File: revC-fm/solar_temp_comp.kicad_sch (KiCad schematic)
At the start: 19 parts, among them U35 ATL431BQ, U36 LT6004HMS8, U37 LT3010-5, U38 ATL431BQ

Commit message: routing
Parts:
- C139: renamed from C125; footprint Capacitor_SMD:C_0402_1005Metric -> Capacitor_SMD:C_0603_1608Metric
- renumbered C122 to C136, C123 to C137, C124 to C138, R246 to R237, R253 to R238, R243 to R239, R248 to R240, R244 to R241, R249 to R242, R245 to R243, R250 to R244, U37 to U38, U36 to U39, U35 to U40, U38 to U41

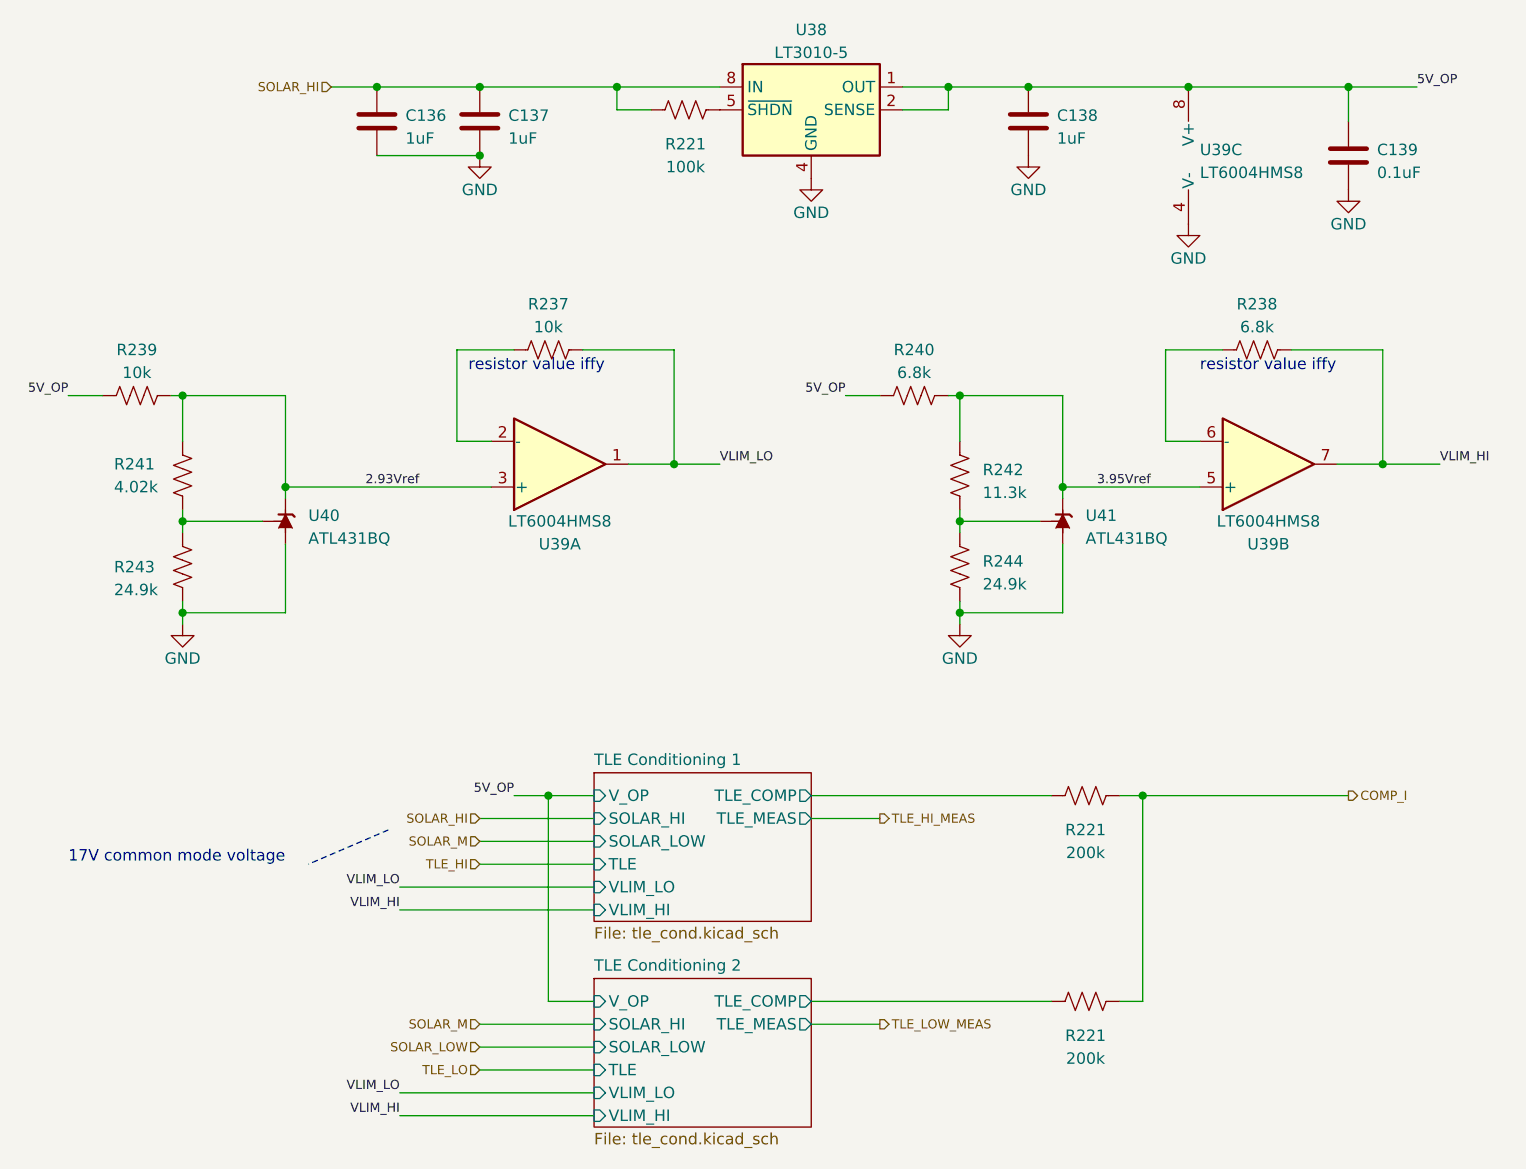
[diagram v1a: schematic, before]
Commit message: changed RF connector to TH
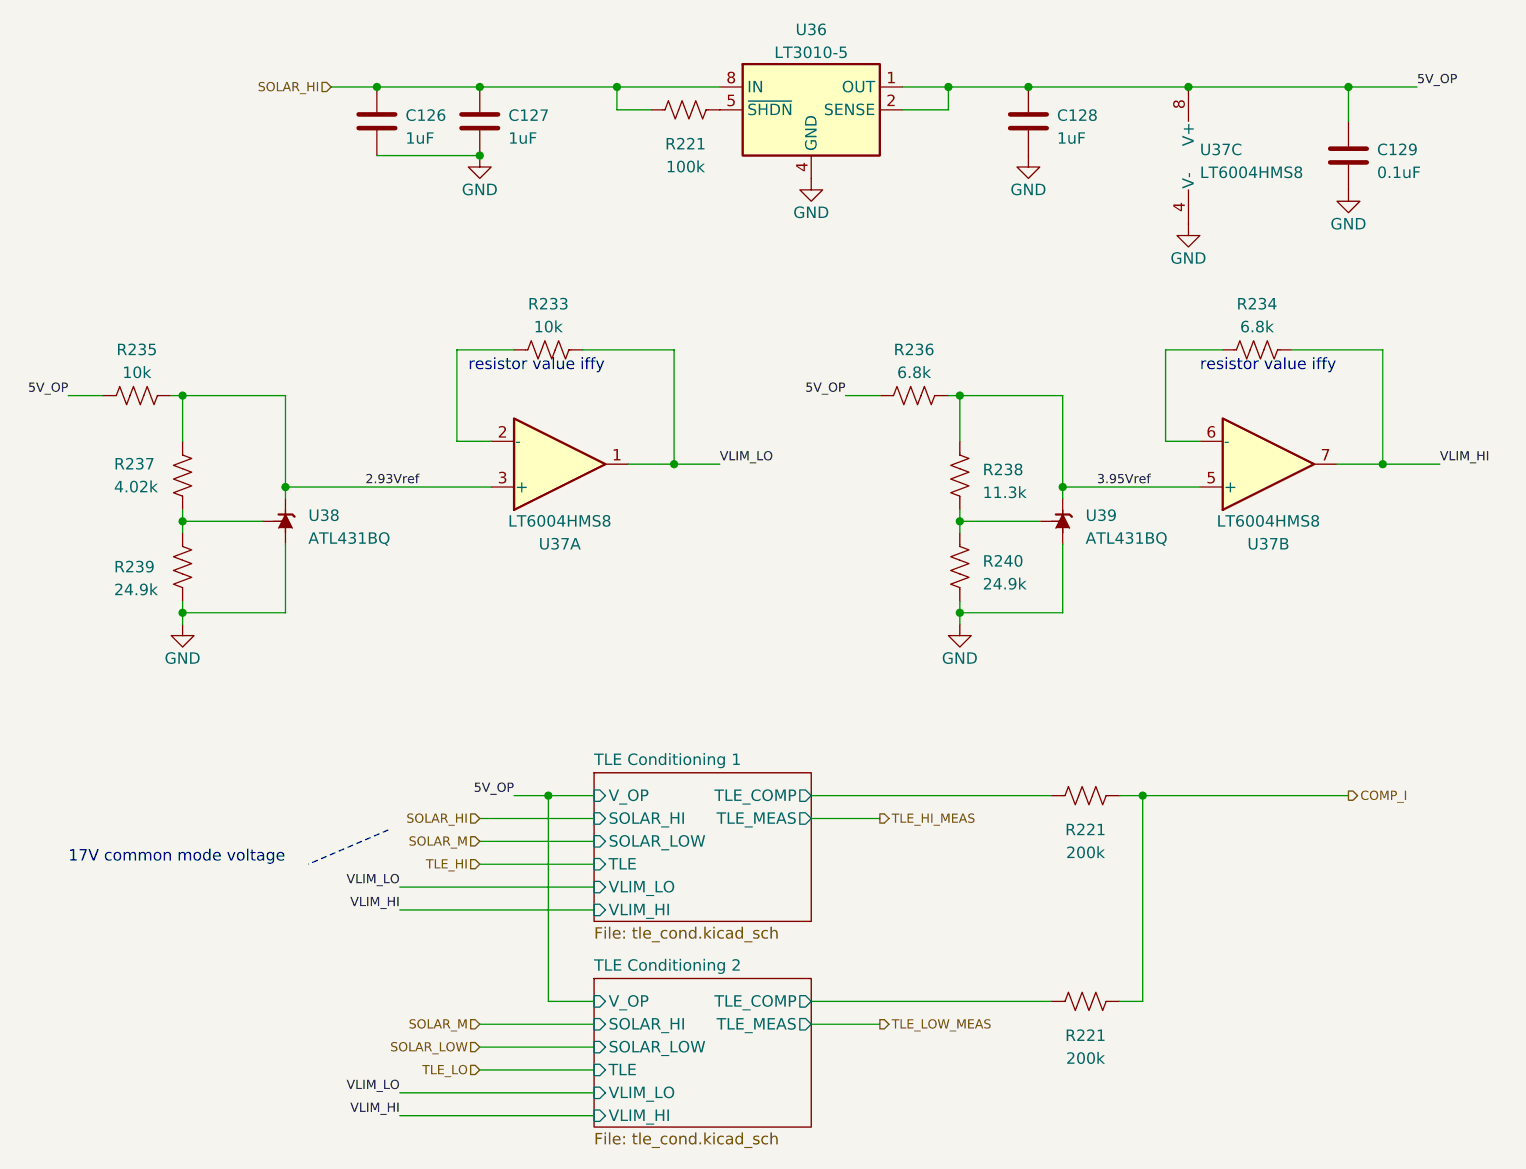
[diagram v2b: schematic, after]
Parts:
- renumbered C136 to C126, C137 to C127, C138 to C128, C139 to C129, R237 to R233, R238 to R234, R239 to R235, R240 to R236, R241 to R237, R242 to R238, R243 to R239, R244 to R240, U38 to U36, U39 to U37, U40 to U38, U41 to U39

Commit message: working revC review changes
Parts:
- renumbered C126 to C127, C127 to C128, C128 to C129, C129 to C130, R233 to R250, R234 to R251, R235 to R252, R236 to R253, R237 to R254, R238 to R255, R239 to R256, R240 to R257, U36 to U37, U37 to U38, U38 to U39, U39 to U40

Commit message: working revC
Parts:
- removed C127, C128: 1uF, Capacitor_SMD:C_0805_2012Metric, symbol Device:C
- removed C129: 1uF, Capacitor_SMD:C_0603_1608Metric, symbol Device:C
- removed C130: 0.1uF, Capacitor_SMD:C_0603_1608Metric, symbol Device:C
- removed R221: 100k, Resistor_SMD:R_0603_1608Metric, symbol Device:R_US
- removed R221: 200k, Resistor_SMD:R_0603_1608Metric, symbol Device:R_US
- removed R250, R252: 10k, Resistor_SMD:R_0603_1608Metric, symbol Device:R_US
- removed R251, R253: 6.8k, Resistor_SMD:R_0603_1608Metric, symbol Device:R_US
- removed R254: 4.02k, Resistor_SMD:R_0603_1608Metric, symbol Device:R_US
- removed R255: 11.3k, Resistor_SMD:R_0603_1608Metric, symbol Device:R_US
- removed R256, R257: 24.9k, Resistor_SMD:R_0603_1608Metric, symbol Device:R_US
- removed U37: LT3010-5, Package_SO:MSOP-8-1EP_3x3mm_P0.65mm_EP1.68x1.88mm, symbol Regulator_Linear:LT3010-5
- removed U38: LT6004HMS8, Package_SO:MSOP-8_3x3mm_P0.65mm, symbol SierraLobo:LT6004HMS8
- removed U39, U40: ATL431BQ, Package_TO_SOT_SMD:SOT-23, symbol SierraLobo:ATL431BQ
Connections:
- net COMP_I: no longer R221.2
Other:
- removed sheet TLE Conditioning 1
- note removed: "resistor value iffy"
